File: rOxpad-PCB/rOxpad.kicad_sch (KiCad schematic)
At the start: 24 parts, among them SW1 SW_Push, U1 ATmega16U2-A, U2 PRTR5V0U2X, Y1 16MHz

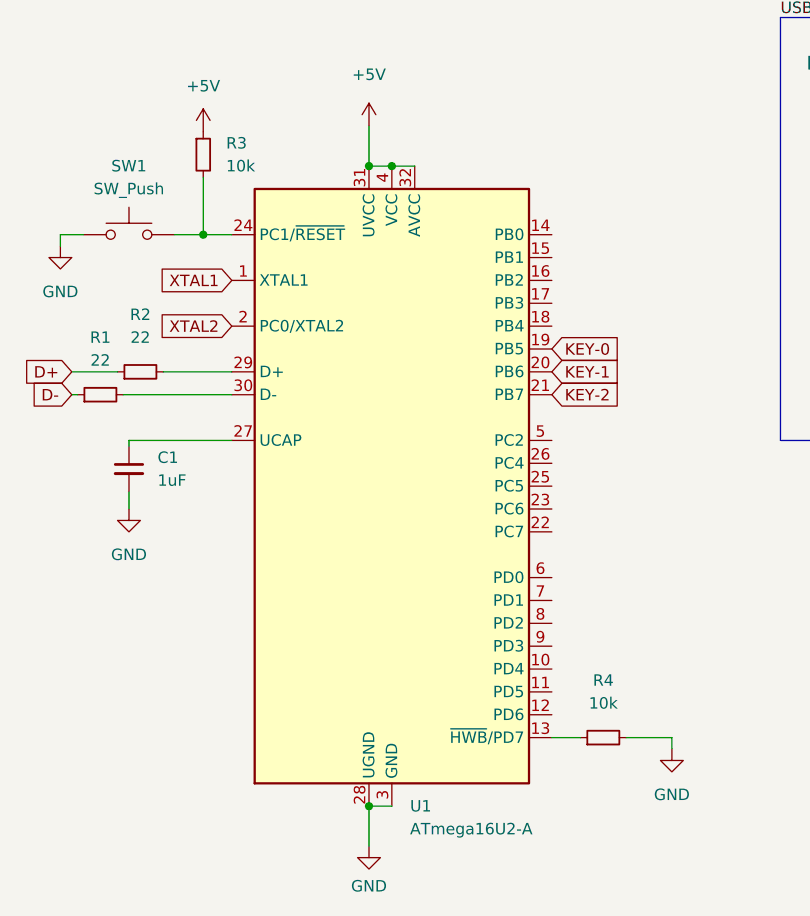
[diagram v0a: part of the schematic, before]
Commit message: change MCU to atmega32u2
a lot cheaper
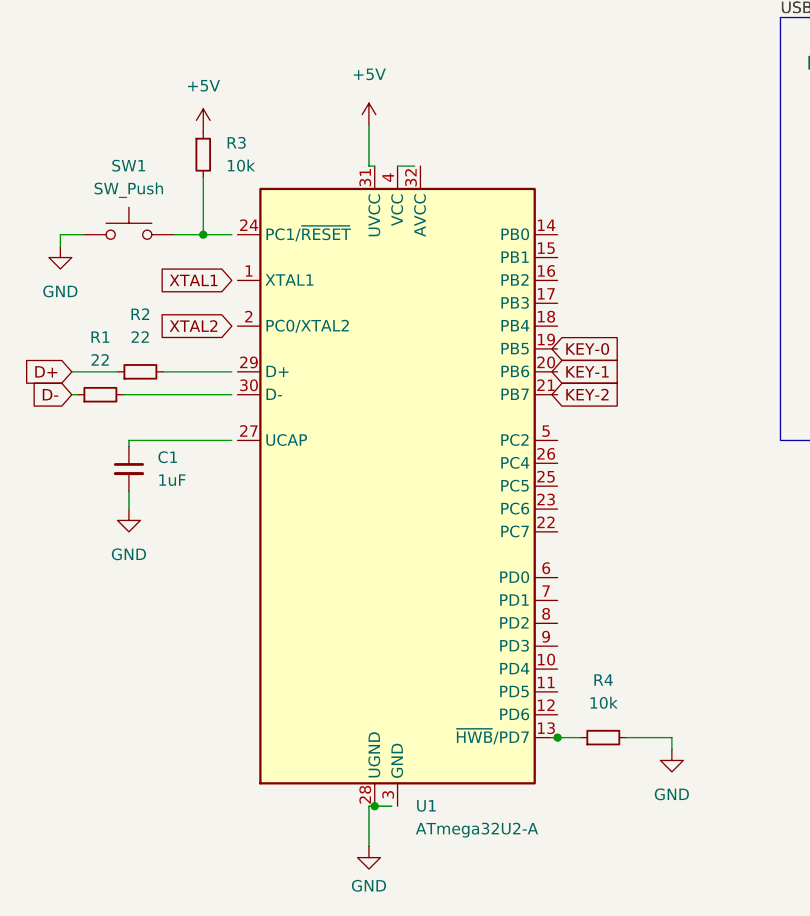
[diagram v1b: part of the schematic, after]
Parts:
- removed U1: ATmega16U2-A, Package_QFP:TQFP-32_7x7mm_P0.8mm, symbol MCU_Microchip_ATmega:ATmega16U2-A
- added U1: ATmega32U2-A, Package_QFP:TQFP-32_7x7mm_P0.8mm, symbol MCU_Microchip_ATmega:ATmega32U2-A
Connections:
- net +5V: now also U1.31 (UVCC)
- net GND: now also U1.28 (UGND)
- net at R4.1: now also U1.13 (~{HWB}/PD7)
